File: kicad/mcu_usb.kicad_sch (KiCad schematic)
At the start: 40 parts, among them J4 USB-A host, SW2 BOOT, U10 RP2354A, U11 SRV05-4, U6 SRV05-4, Y1 12MHz

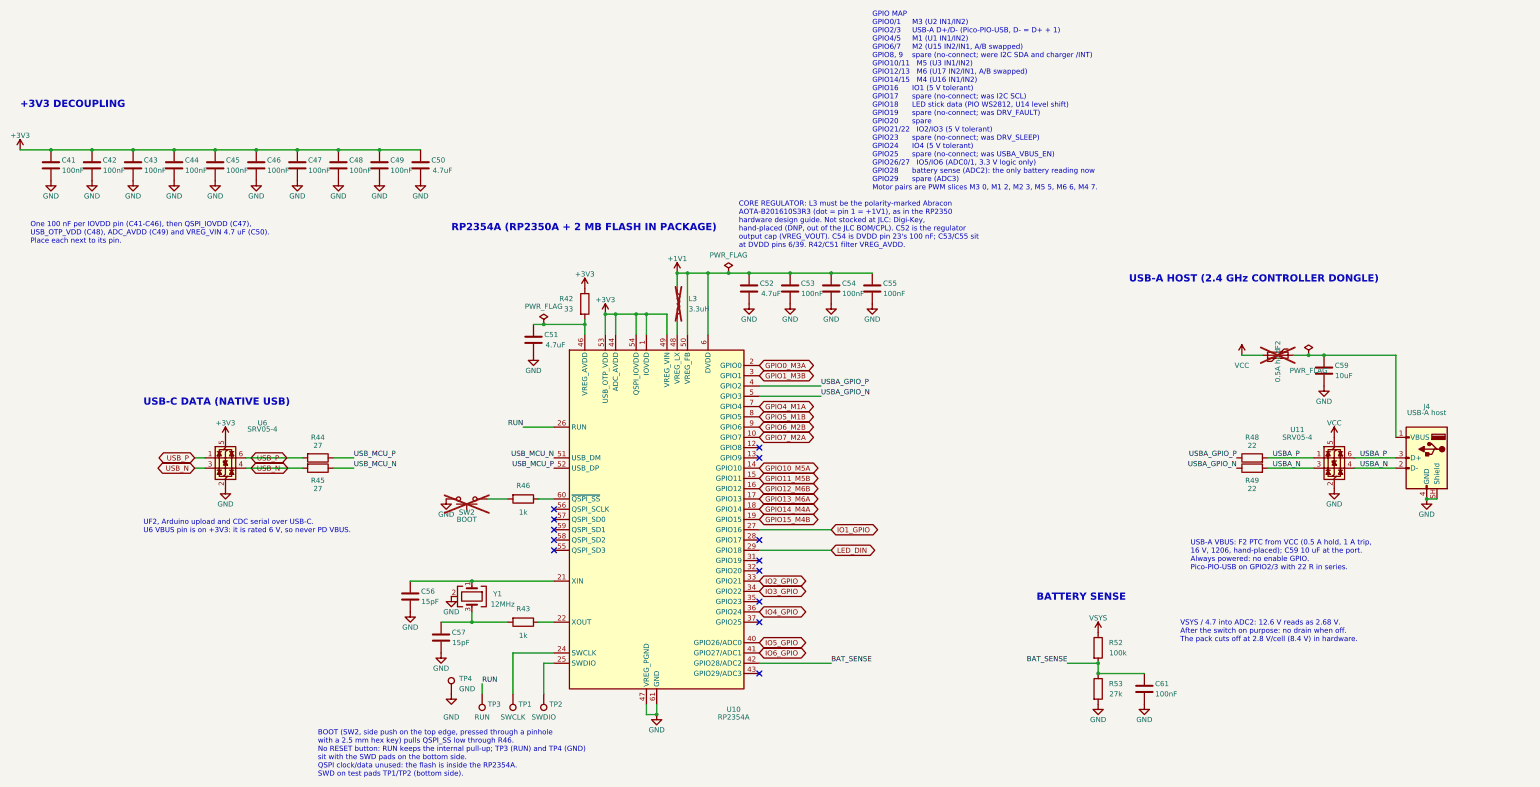
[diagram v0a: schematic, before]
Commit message: Place the brain double-sided at 66.3 x 34 mm, unrouted
- tools/place_double.py rebuilds the placement from scratch: parts on both
  sides, M1-M6 swapped to JST PH S2B-PH-K (C173752), J3 under J4, the
  switches in the bottom-right corner, the USB-C ESD and series resistors
  on the front between J1 and U10.
- Pulls in the 2026-10-20 schematic change (IO5/IO6 off the ADC pins,
  R109/R114 15k USB-A pull-downs).
- Reassigns U10 GPIOs for the new layout, keeping each motor on its own
  PWM slice and IO4-IO6 on slices 1 and 4; USB-A moves to GPIO26/27.
- Adds back-side fiducials FID4-FID6.
- The old partial autoroute is kept in kicad/reference/.

Co-Authored-By: Claude Opus 5.5 <noreply@anthropic.com>
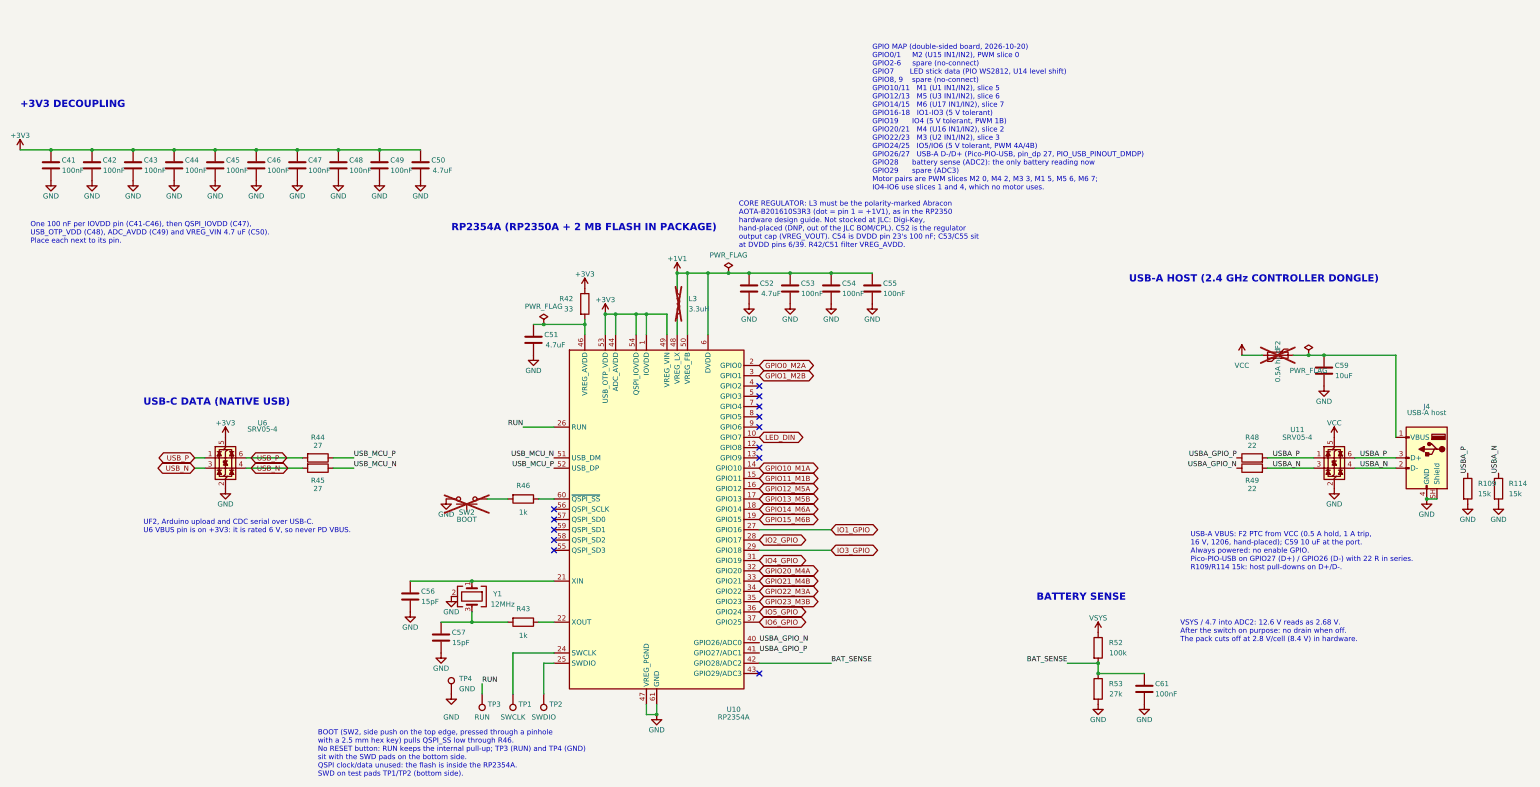
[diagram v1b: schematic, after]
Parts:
- added R109, R114: 15k, Resistor_SMD:R_0402_1005Metric, symbol Device:R
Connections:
- net GPIO7_M2A is gone; now on net LED_DIN: U10.10 (GPIO7)
- net GND: now also R109.2, R114.2
- net IO2_GPIO: now also U10.28 (GPIO17); no longer U10.33 (GPIO21)
- net IO3_GPIO: now also U10.29 (GPIO18); no longer U10.34 (GPIO22)
- net IO4_GPIO: now also U10.31 (GPIO19); no longer U10.36 (GPIO24)
- net IO5_GPIO: now also U10.36 (GPIO24); no longer U10.40 (GPIO26/ADC0)
- net IO6_GPIO: now also U10.37 (GPIO25); no longer U10.41 (GPIO27/ADC1)
- net LED_DIN: no longer U10.29 (GPIO18)
- net USBA_GPIO_N: now also U10.40 (GPIO26/ADC0); no longer U10.5 (GPIO3)
- net USBA_GPIO_P: now also U10.41 (GPIO27/ADC1); no longer U10.4 (GPIO2)
- net USBA_N: now also R114.1
- net USBA_P: now also R109.1
- net GPIO20_M4A: now reaches U10.32 (GPIO20)
- net GPIO23_M3B: now reaches U10.35 (GPIO23)
- net GPIO0_M3A renamed GPIO0_M2A
- net GPIO10_M5A renamed GPIO10_M1A
- net GPIO11_M5B renamed GPIO11_M1B
- net GPIO12_M6B renamed GPIO12_M5A
- net GPIO13_M6A renamed GPIO13_M5B
- net GPIO14_M4A renamed GPIO14_M6A
- net GPIO15_M4B renamed GPIO15_M6B
- net GPIO1_M3B renamed GPIO1_M2B
- net GPIO4_M1A: no longer names the net of U10.7 (GPIO4)
- net GPIO5_M1B: no longer names the net of U10.8 (GPIO5)
- net GPIO6_M2B: no longer names the net of U10.9 (GPIO6)
- new net GPIO21_M4B: U10.33 (GPIO21)
- new net GPIO22_M3A: U10.34 (GPIO22)
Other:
- note added: "GPIO MAP (double-sided board, 2026-10-20) GPIO0/1 M2 (U15 IN1/IN2), PWM slice 0 GPIO2-6 spare (no-connect) GPIO7 LED stick data (PIO WS2812, U14 level shift) GPIO8, 9 spare (no-connect) GPIO10/11 M1 (U1 IN1/IN2), slice 5 GPIO12/13 M5 (U3 IN1/IN2), slice 6 GPIO14/15 M6 (U17 IN1/IN2), slice 7 GPIO16-18 IO1-IO3 (5 V tolerant) GPIO19 IO4 (5 V tolerant, PWM 1B) GPIO20/21 M4 (U16 IN1/IN2), slice 2 GPIO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"
- note added: "USB-A VBUS: F2 PTC from VCC (0.5 A hold, 1 A trip, 16 V, 1206, hand-placed); C59 10 uF at the port. Always powered: no enable GPIO. Pico-PIO-USB on GPIO27 (D+) / GPIO26 (D-) with 22 R in series. R109/R114 15k: host pull-downs on D+/D-."
- note removed: "GPIO MAP GPIO0/1 M3 (U2 IN1/IN2) GPIO2/3 USB-A D+/D- (Pico-PIO-USB, D- = D+ + 1) GPIO4/5 M1 (U1 IN1/IN2) GPIO6/7 M2 (U15 IN2/IN1, A/B swapped) GPIO8, 9 spare (no-connect; were I2C SDA and charger /INT) GPIO10/11 M5 (U3 IN1/IN2) GPIO12/13 M6 (U17 IN2/IN1, A/B swapped) GPIO14/15 M4 (U16 IN1/IN2) GPIO16 IO1 (5 V tolerant) GPIO17 spare (no-connect; was I2C SCL) GPIO18 LED stick data (PIO WS2812, U14 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"
- note removed: "USB-A VBUS: F2 PTC from VCC (0.5 A hold, 1 A trip, 16 V, 1206, hand-placed); C59 10 uF at the port. Always powered: no enable GPIO. Pico-PIO-USB on GPIO2/3 with 22 R in series."

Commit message: Rotate U10 to 0 deg and re-place the brain at 66.6 x 32 mm, unrouted
USB now runs straight down from J1 into U10's north pins; IO goes west to J5,
which moves to the top of the left wall with M5/M6 below it. SW1 sits under
U16 and SW2 in the bottom-right corner; Q1 is east of J3. GPIO map redone for
the new orientation (IO1-6 on GPIO0-3/8/9, motors on GPIO12-17/20-23/26-27,
USB-A on GPIO24/25, LED on GPIO29). ERC clean, DRC parity clean.

Co-Authored-By: Claude Opus 5.5 <noreply@anthropic.com>
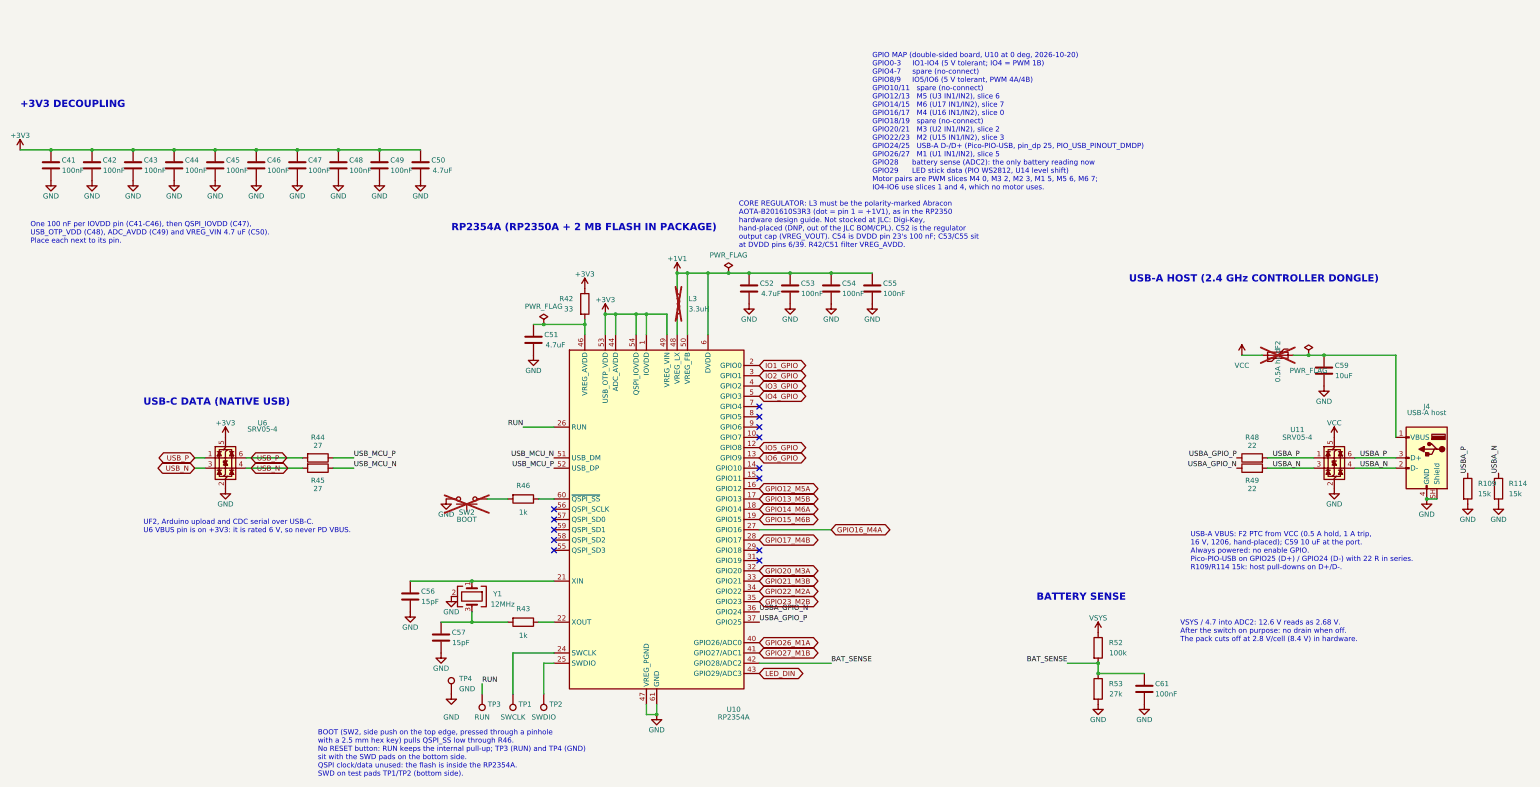
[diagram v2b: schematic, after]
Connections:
- net GPIO0_M2A is gone; now on net IO1_GPIO: U10.2 (GPIO0)
- net GPIO1_M2B is gone; now on net IO2_GPIO: U10.3 (GPIO1)
- net IO1_GPIO: no longer U10.27 (GPIO16)
- net IO2_GPIO: no longer U10.28 (GPIO17)
- net IO3_GPIO: now also U10.4 (GPIO2); no longer U10.29 (GPIO18)
- net IO4_GPIO: now also U10.5 (GPIO3); no longer U10.31 (GPIO19)
- net IO5_GPIO: now also U10.12 (GPIO8); no longer U10.36 (GPIO24)
- net IO6_GPIO: now also U10.13 (GPIO9); no longer U10.37 (GPIO25)
- net LED_DIN: now also U10.43 (GPIO29/ADC3); no longer U10.10 (GPIO7)
- net USBA_GPIO_N: now also U10.36 (GPIO24); no longer U10.40 (GPIO26/ADC0)
- net USBA_GPIO_P: now also U10.37 (GPIO25); no longer U10.41 (GPIO27/ADC1)
- net GPIO10_M1A: no longer names the net of U10.14 (GPIO10)
- net GPIO11_M1B: no longer names the net of U10.15 (GPIO11)
- net GPIO20_M4A renamed GPIO20_M3A
- net GPIO21_M4B renamed GPIO21_M3B
- net GPIO22_M3A renamed GPIO22_M2A
- net GPIO23_M3B renamed GPIO23_M2B
- new net GPIO16_M4A: U10.27 (GPIO16)
- new net GPIO17_M4B: U10.28 (GPIO17)
- new net GPIO26_M1A: U10.40 (GPIO26/ADC0)
- new net GPIO27_M1B: U10.41 (GPIO27/ADC1)
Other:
- note added: "GPIO MAP (double-sided board, U10 at 0 deg, 2026-10-20) GPIO0-3 IO1-IO4 (5 V tolerant; IO4 = PWM 1B) GPIO4-7 spare (no-connect) GPIO8/9 IO5/IO6 (5 V tolerant, PWM 4A/4B) GPIO10/11 spare (no-connect) GPIO12/13 M5 (U3 IN1/IN2), slice 6 GPIO14/15 M6 (U17 IN1/IN2), slice 7 GPIO16/17 M4 (U16 IN1/IN2), slice 0 GPIO18/19 spare (no-connect) GPIO20/21 M3 (U2 IN1/IN2), slice 2 GPIO22/23 M2 (U15 IN1/IN2), s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"
- note added: "USB-A VBUS: F2 PTC from VCC (0.5 A hold, 1 A trip, 16 V, 1206, hand-placed); C59 10 uF at the port. Always powered: no enable GPIO. Pico-PIO-USB on GPIO25 (D+) / GPIO24 (D-) with 22 R in series. R109/R114 15k: host pull-downs on D+/D-."
- note removed: "GPIO MAP (double-sided board, 2026-10-20) GPIO0/1 M2 (U15 IN1/IN2), PWM slice 0 GPIO2-6 spare (no-connect) GPIO7 LED stick data (PIO WS2812, U14 level shift) GPIO8, 9 spare (no-connect) GPIO10/11 M1 (U1 IN1/IN2), slice 5 GPIO12/13 M5 (U3 IN1/IN2), slice 6 GPIO14/15 M6 (U17 IN1/IN2), slice 7 GPIO16-18 IO1-IO3 (5 V tolerant) GPIO19 IO4 (5 V tolerant, PWM 1B) GPIO20/21 M4 (U16 IN1/IN2), slice 2 GPIO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"
- note removed: "USB-A VBUS: F2 PTC from VCC (0.5 A hold, 1 A trip, 16 V, 1206, hand-placed); C59 10 uF at the port. Always powered: no enable GPIO. Pico-PIO-USB on GPIO27 (D+) / GPIO26 (D-) with 22 R in series. R109/R114 15k: host pull-downs on D+/D-."

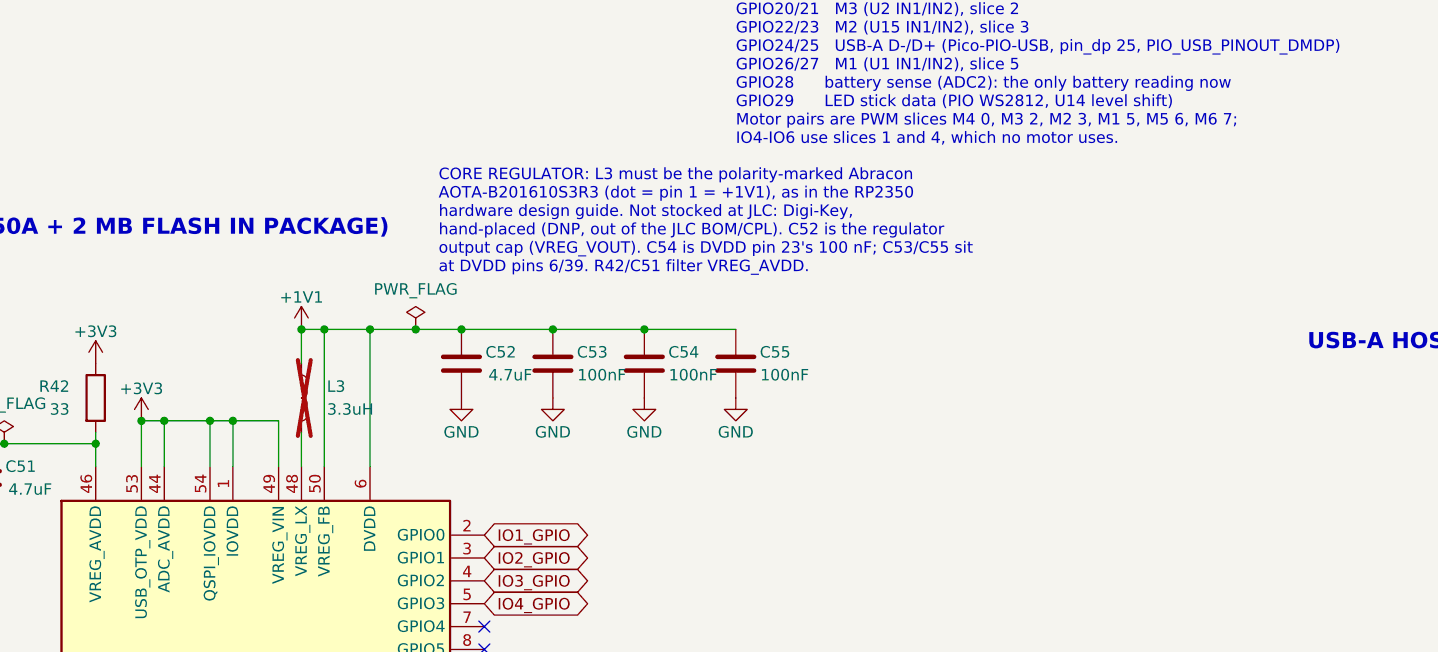
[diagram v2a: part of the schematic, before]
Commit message: Replace the RP2354 core inductor with a 1.1 V LDO and fix JLC placements
L3 (the Abracon AOTA-B201610S3R3-101-T, the only polarity-marked inductor
RPi approves) had 3 in stock at JLC. DVDD now comes from U12, a TLV74311
LDO on +3V3 with C87/C86, as in RP2350 datasheet Fig. 24: VREG_FB to GND,
VREG_LX open, VREG_VIN and VREG_AVDD still powered. Firmware must set the
VREG HIZ bit after boot and never use the regulator's low-power mode.

- Schematic, placement, recipe, grid router and DRU updated; the copper
  is rebuilt with route_all. DRC, ERC and parity are clean.
- fab.py: JLC rotation offsets for the JST PH connectors, J3's XT30 and
  SW1 (all 180 degrees), and U8 placed at its pad centre, from JLC's
  placement preview. The JLC quote is $269.19 for 5 panels.
- Unused footprints removed (L_Abracon_AOTA-B201610, the trimmed 0402),
  along with the cleanup session's footprint, symbol, branch and build/
  tidy-up, and its renders/, docs/ and tools/case/ moves.

Co-Authored-By: Claude Opus 5.5 <noreply@anthropic.com>
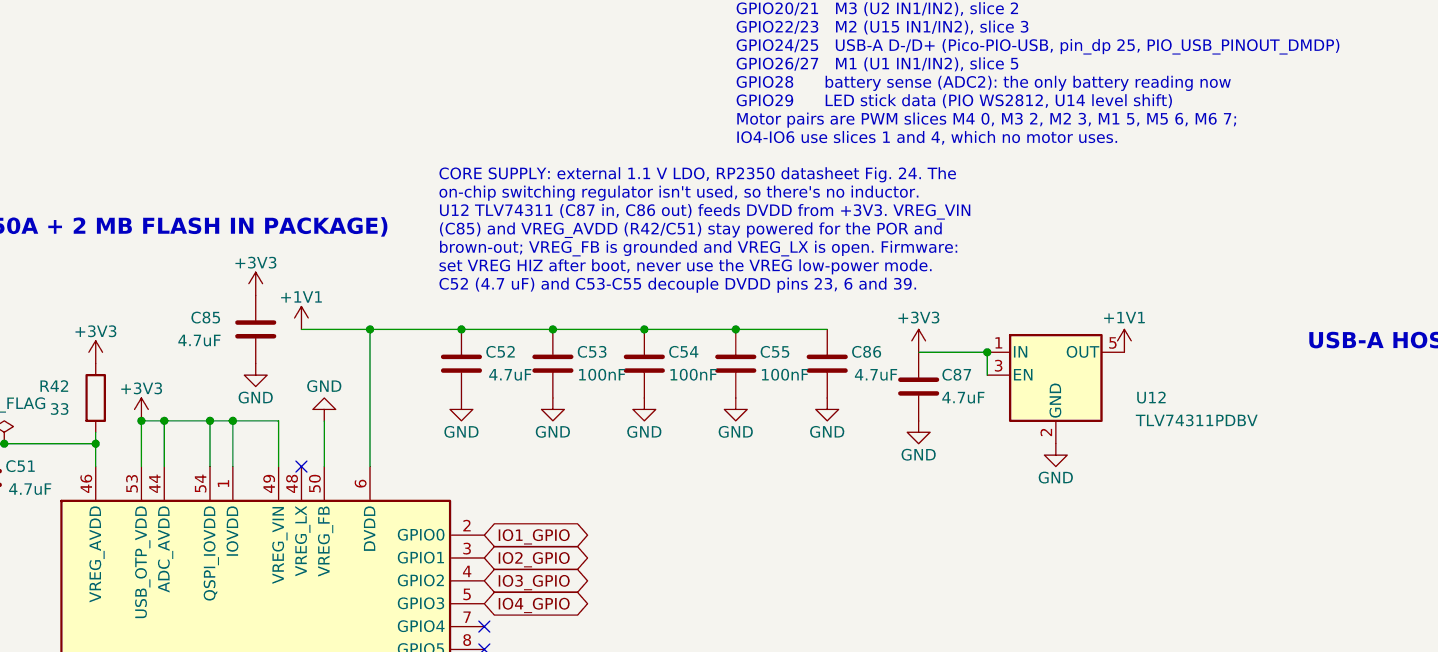
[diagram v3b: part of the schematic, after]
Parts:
- removed L3: 3.3uH, hexy:L_Abracon_AOTA-B201610, symbol Device:L
- added C85, C86, C87: 4.7uF, Capacitor_SMD:C_0402_1005Metric, symbol Device:C
- added U12: TLV74311PDBV, Package_TO_SOT_SMD:SOT-23-5, symbol hexyhustle:TLV74311PDBV
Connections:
- net +1V1: now also C86.1, U12.5 (OUT); no longer U10.50 (VREG_FB)
- net +3V3: now also C85.1, C87.1, U12.1 (IN), U12.3 (EN)
- net GND: now also U10.50 (VREG_FB), C85.2, C86.2, C87.2, U12.2 (GND)
- no-connect marks 13 -> 14
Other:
- note added: "CORE SUPPLY: external 1.1 V LDO, RP2350 datasheet Fig. 24. The on-chip switching regulator isn't used, so there's no inductor. U12 TLV74311 (C87 in, C86 out) feeds DVDD from +3V3. VREG_VIN (C85) and VREG_AVDD (R42/C51) stay powered for the POR and brown-out; VREG_FB is grounded and VREG_LX is open. Firmware: set VREG HIZ after boot, never use the VREG low-power mode. C52 (4.7 uF) and C53-C55 deco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"
- note removed: "CORE REGULATOR: L3 must be the polarity-marked Abracon AOTA-B201610S3R3 (dot = pin 1 = +1V1), as in the RP2350 hardware design guide. Not stocked at JLC: Digi-Key, hand-placed (DNP, out of the JLC BOM/CPL). C52 is the regulator output cap (VREG_VOUT). C54 is DVDD pin 23's 100 nF; C53/C55 sit at DVDD pins 6/39. R42/C51 filter VREG_AVDD."

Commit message: Have JLC place SW2, D4, U14 and F2, and shift U8 onto its model
- SW2 (BOOT), D4, U14 and F2 were DNP for hand placement. All four are
  in stock at JLC, so they're placed now (DNP cleared in the schematic
  and on the board). The JLC BOM grows from 47 to 51 lines.
- fab.py: JLC's SOT-89-3 model for U8 (C16106) sits 0.474 mm toward the
  tab from its footprint origin, so U8's CPL point moves that far toward
  its pins (JLC_PART_SHIFT), replacing the pad-centre approximation.
- The 10-panel JLC quote is $331.69, and the preview shows all five parts
  correct.

Co-Authored-By: Claude Opus 5.5 <noreply@anthropic.com>
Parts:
- F2, SW2: now fitted
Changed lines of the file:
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@@
 		(on_board yes)
 		(in_pos_files yes)
-		(dnp yes)
+		(dnp no)
 		(property "Reference" "F2"
 			(at 344.17 111.76 0)
@@
 		(on_board yes)
 		(in_pos_files yes)
-		(dnp yes)
+		(dnp no)
 		(property "Reference" "SW2"
 			(at 143.51 153.16 0)
